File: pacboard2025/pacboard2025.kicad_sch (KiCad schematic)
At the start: 31 parts, among them J1 XT30 Male Connector, U2 D24V50F5, U3 ProS3

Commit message: some more changes
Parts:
- renumbered INTR_TOF to INTR_TOF1, XSHUT_TOF to XSHUT_TOF1
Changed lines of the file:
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@@
 		(on_board yes)
 		(dnp no)
-		(property "Reference" "INTR_TOF"
+		(property "Reference" "INTR_TOF1"
 			(at 35.306 140.716 0)
 			(effects
@@
 			(project "pacboard2025"
 				(path "/8e380e0f-b63e-4626-b5ee-6ded4a9a683b"
-					(reference "INTR_TOF")
+					(reference "INTR_TOF1")
 					(unit 1)
 				)
@@
 		(on_board yes)
 		(dnp no)
-		(property "Reference" "XSHUT_TOF"
+		(property "Reference" "XSHUT_TOF1"
 			(at 30.734 118.872 0)
 			(effects
@@
 			(project "pacboard2025"
 				(path "/8e380e0f-b63e-4626-b5ee-6ded4a9a683b"
-					(reference "XSHUT_TOF")
-					(unit 1)
-				)
+					(reference "XSHUT_TOF1")
+					(unit 1)
+				)

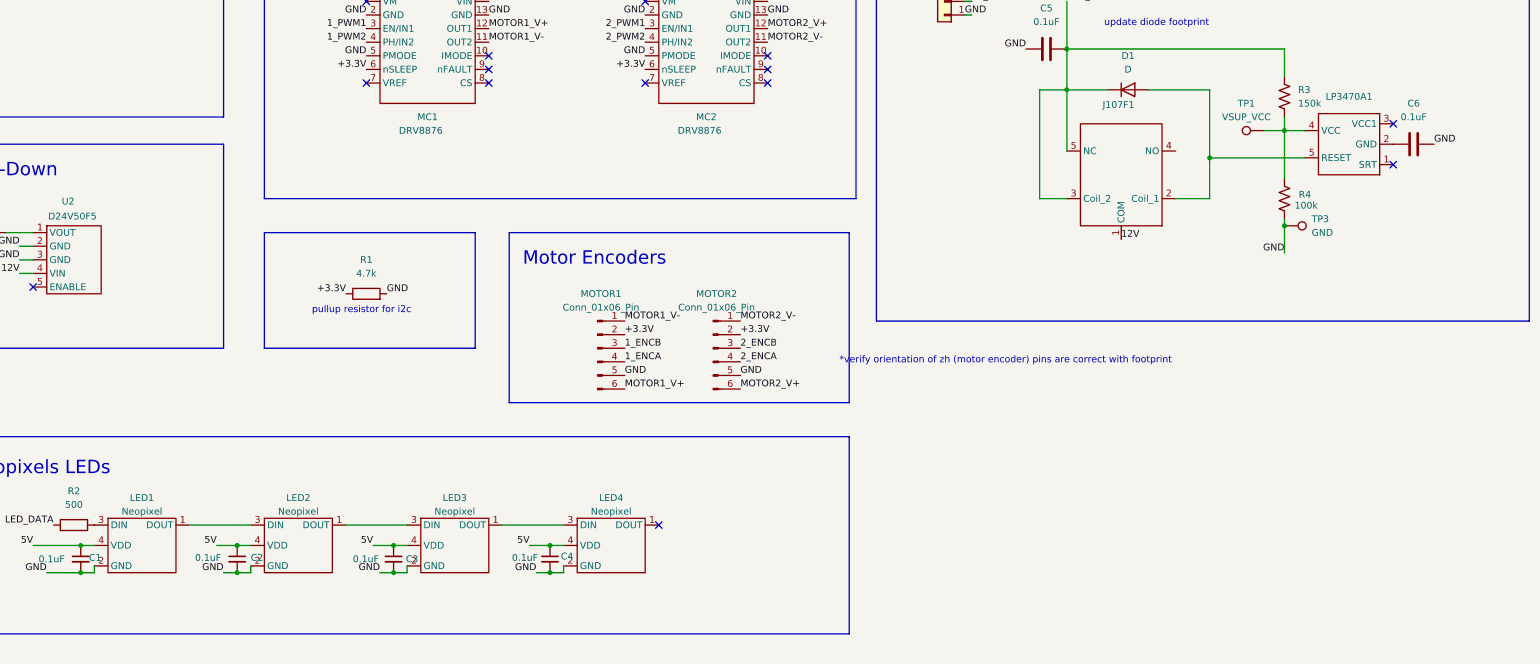
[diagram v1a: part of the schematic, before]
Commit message: fixed neopixels, all ready to go?
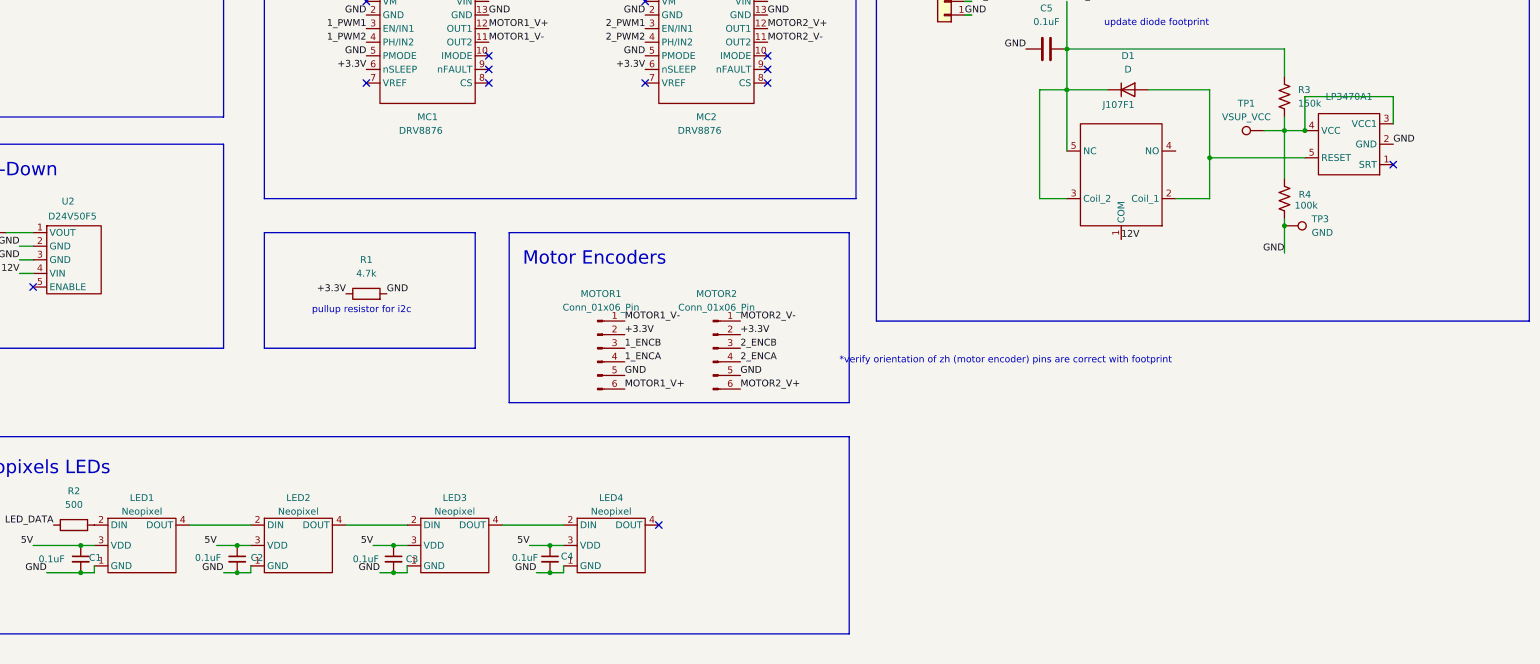
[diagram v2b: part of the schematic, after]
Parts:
- removed C6: 0.1uF, Capacitor_SMD:C_0805_2012Metric_Pad1.18x1.45mm_HandSolder, symbol Device:C
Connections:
- net 5V: now also LED1.3 (VDD), LED2.3 (VDD), LED3.3 (VDD), LED4.3 (VDD); no longer LED1.4 (VDD), LED2.4 (VDD), LED3.4 (VDD), LED4.4 (VDD)
- net GND: now also LED1.1 (GND), LED2.1 (GND), LED3.1 (GND), LED4.1 (GND), LP3470A1.2 (GND); no longer LED1.2 (GND), LED2.2 (GND), LED3.2 (GND), LED4.2 (GND)
- net at R2.2: now also LED1.2 (DIN); no longer LED1.3 (DIN)
- net at LP3470A1.4 (VCC), R3.2, R4.1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: now also LP3470A1.3 (VCC1)
- new net: LED2.4 (DOUT), LED3.2 (DIN)
- new net: LED3.4 (DOUT), LED4.2 (DIN)
- new net: LED1.4 (DOUT), LED2.2 (DIN)
- no-connect marks 19 -> 18
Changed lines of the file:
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@@
 	)
 	(junction
+		(at 359.41 62.23)
+		(diameter 0)
+		(color 0 0 0 0)
+	)
+	(junction
 		(at 130.81 144.78)
 		(diameter 0)
@@
 	)
 	(no_connect
-		(at 375.92 60.96)
-	)
-	(no_connect
 		(at 236.22 53.34)
 	)
@@
 	(wire
 		(pts
+			(xy 375.92 60.96) (xy 375.92 55.88)
+		)
+		(stroke
+			(width 0)
+			(type default)
+		)
+	)
+	(wire
+		(pts
 			(xy 121.92 83.82) (xy 119.38 83.82)
 		)
@@
 	(wire
 		(pts
+			(xy 375.92 55.88) (xy 359.41 55.88)
+		)
+		(stroke
+			(width 0)
+			(type default)
+		)
+	)
+	(wire
+		(pts
 			(xy 105.41 81.28) (xy 109.22 81.28)
 		)
@@
 	(wire
 		(pts
+			(xy 359.41 55.88) (xy 359.41 62.23)
+		)
+		(stroke
+			(width 0)
+			(type default)
+		)
+	)
+	(wire
+		(pts
 			(xy 341.63 67.31) (xy 341.63 74.93)
 		)
@@
 	)
 	(label "GND"
-		(at 383.54 64.77 0)
+		(at 375.92 64.77 0)
 		(fields_autoplaced yes)
 		(effects
@@
 	)
 	(symbol
-		(lib_id "Device:C")
-		(at 379.73 64.77 90)
-		(unit 1)
-		(exclude_from_sim no)
-		(in_bom yes)
-		(on_board yes)
-		(dnp no)
-		(fields_autoplaced yes)
-		(property "Reference" "C6"
-			(at 379.73 57.15 90)
-			(effects
-				(font
-					(size 1.27 1.27)
-				)
-			)
-		)
-		(property "Value" "0.1uF"
-			(at 379.73 59.69 90)
-			(effects
-				(font
-					(size 1.27 1.27)
-				)
-			)
-		)
-		(property "Footprint" "Capacitor_SMD:C_0805_2012Metric_Pad1.18x1.45mm_HandSolder"
-			(at 383.54 63.8048 0)
-			(effects
-				(font
-					(size 1.27 1.27)
-				)
-				(hide yes)
-			)
-		)
-		(property "Datasheet" "~"
-			(at 379.73 64.77 0)
-			(effects
-				(font
-					(size 1.27 1.27)
-				)
-				(hide yes)
-			)
-		)
-		(property "Description" "Unpolarized capacitor"
-			(at 379.73 64.77 0)
-			(effects
-				(font
-					(size 1.27 1.27)
-				)
-				(hide yes)
-			)
-		)
-		(pin "1"
-		)
-		(pin "2"
-		)
-		(instances
-			(project "pacboard2025"
-				(path "/8e380e0f-b63e-4626-b5ee-6ded4a9a683b"
-					(reference "C6")
-					(unit 1)
-				)
-			)
-		)
-	)
-	(symbol
 		(lib_id "Device:R")
 		(at 184.15 92.71 90)
@@
 	)
 	(symbol
+		(lib_name "Neopixel_1")
 		(lib_id "board1_libs:Neopixel")
 		(at 142.24 132.08 0)

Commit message: some more misc changes
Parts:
- LED1, LED2, LED3, LED4: footprint board1_footprints:Neopixel -> board1_footprints:Neopixels 5050
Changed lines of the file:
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@@
 			)
 		)
-		(property "Footprint" "board1_footprints:Neopixel"
+		(property "Footprint" "board1_footprints:Neopixels 5050"
 			(at 200.66 132.08 0)
 			(effects
@@
 			)
 		)
-		(property "Footprint" "board1_footprints:Neopixel"
+		(property "Footprint" "board1_footprints:Neopixels 5050"
 			(at 171.45 132.08 0)
 			(effects
@@
 			)
 		)
-		(property "Footprint" "board1_footprints:Neopixel"
+		(property "Footprint" "board1_footprints:Neopixels 5050"
 			(at 142.24 132.08 0)
 			(effects
@@
 			)
 		)
-		(property "Footprint" "board1_footprints:Neopixel"
+		(property "Footprint" "board1_footprints:Neopixels 5050"
 			(at 229.87 132.08 0)
 			(effects

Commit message: jonathan change bms
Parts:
- D2: footprint board1_footprints:SOD-123FL -> Diode_SMD:D_SMB
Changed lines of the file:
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@@
 			)
 		)
-		(property "Footprint" "board1_footprints:SOD-123FL"
+		(property "Footprint" "Diode_SMD:D_SMB"
 			(at 113.03 81.28 0)
 			(effects

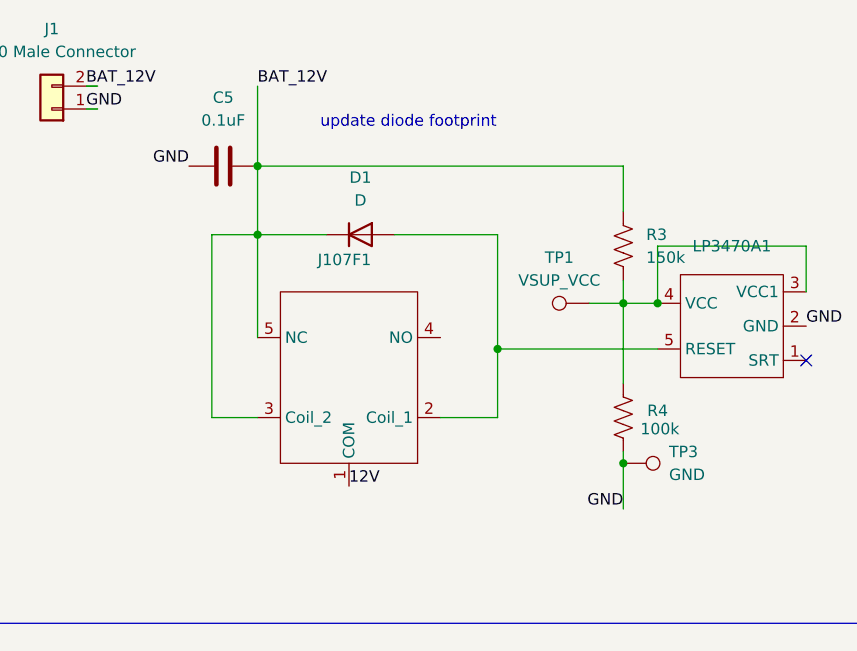
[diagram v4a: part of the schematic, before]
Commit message: updated bms schematic and layout
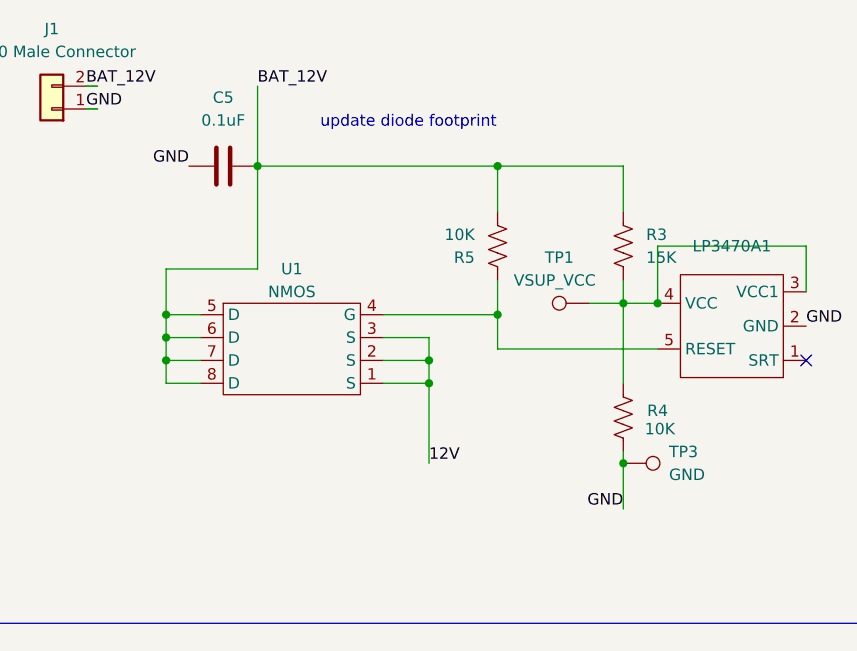
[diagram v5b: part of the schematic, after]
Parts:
- removed D1: D, board1_footprints:SOD-123FL, symbol Device:D
- removed J107F1: ~, board1_footprints:J107, symbol board1_libs:J107F
- added R5: 10K, Resistor_SMD:R_0805_2012Metric_Pad1.20x1.40mm_HandSolder, symbol Device:R_US
- added U1: NMOS, board1_footprints:IFX-PG-TSDSON-8-901-G-V, symbol board1_libs:IRLHM620PbF
- R3: value 150k -> 15K
- R4: value 100k -> 10K
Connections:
- net 12V: now also U1.1 (S), U1.2 (S), U1.3 (S)
- net BAT_12V: now also R5.2, U1.5 (D), U1.6 (D), U1.7 (D), U1.8 (D)
- net at LP3470A1.5 (RESET): now also R5.1, U1.4 (G)

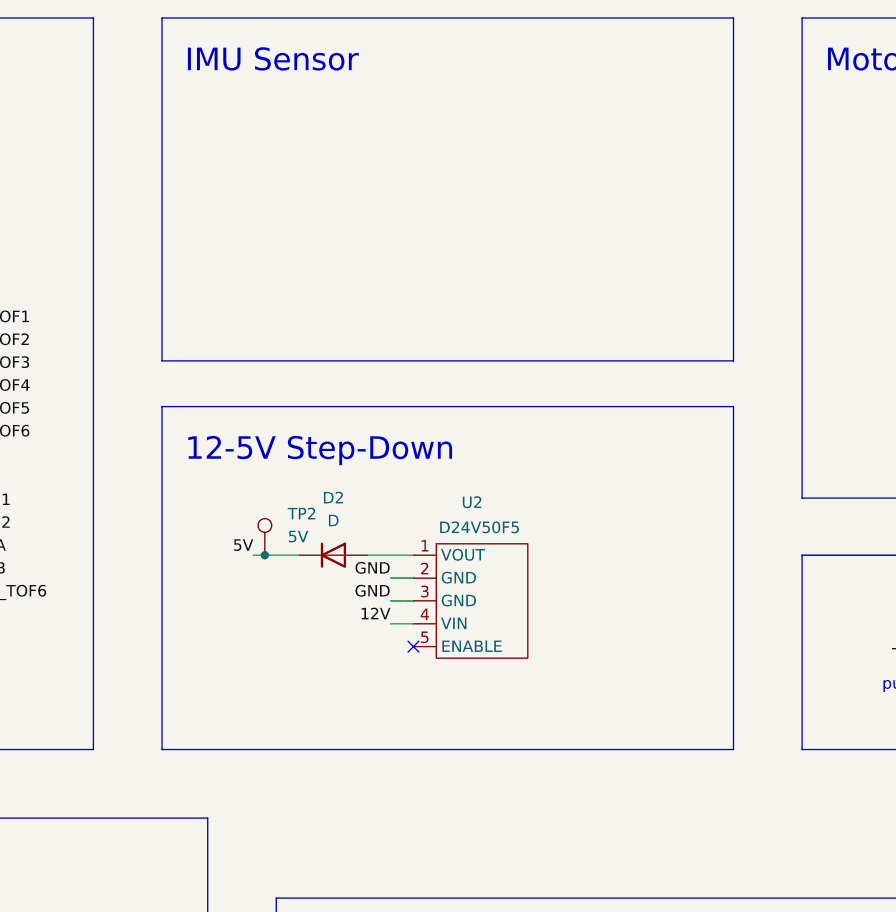
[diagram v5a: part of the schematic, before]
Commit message: final changes, pcb ordered
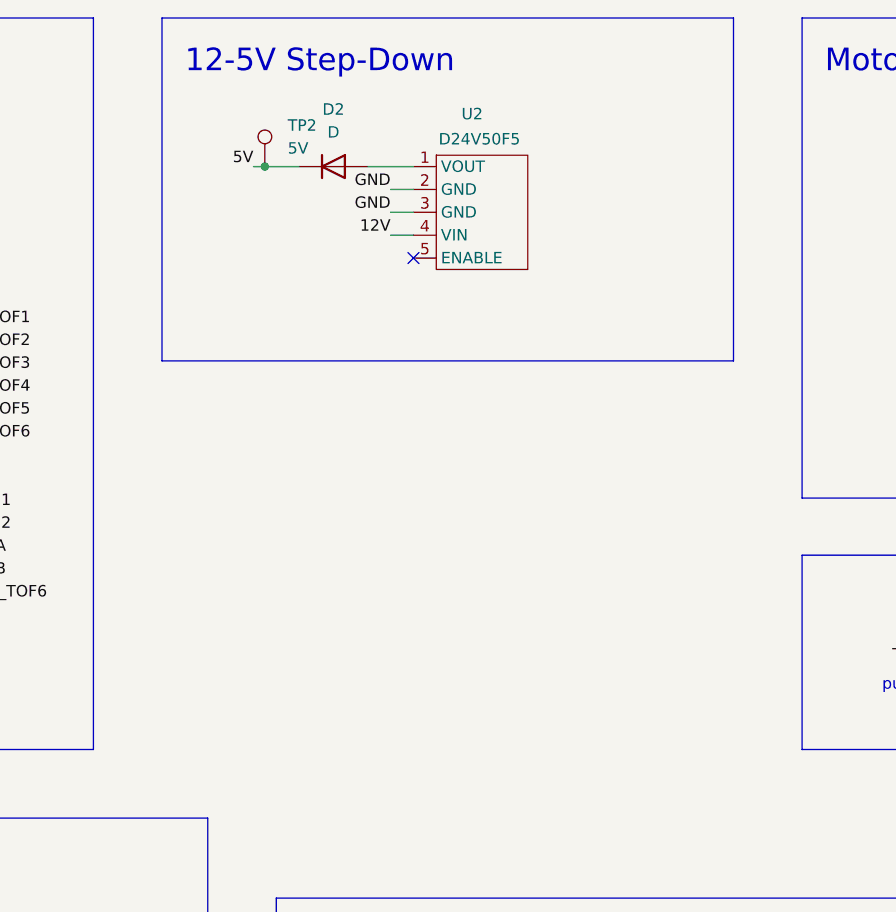
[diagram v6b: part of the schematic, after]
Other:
- note removed: "IMU Sensor"
- moved on the sheet: D2, TP2, U2
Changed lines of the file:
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@@
 	)
 	(junction
-		(at 105.41 81.28)
+		(at 105.41 38.1)
 		(diameter 0)
 		(color 0 0 0 0)
@@
 	)
 	(no_connect
-		(at 121.92 91.44)
+		(at 121.92 48.26)
 	)
 	(no_connect
@@
 	(wire
 		(pts
-			(xy 121.92 86.36) (xy 119.38 86.36)
+			(xy 121.92 43.18) (xy 119.38 43.18)
 		)
 		(stroke
@@
 	(wire
 		(pts
-			(xy 121.92 83.82) (xy 119.38 83.82)
+			(xy 121.92 40.64) (xy 119.38 40.64)
 		)
 		(stroke
@@
 	(wire
 		(pts
-			(xy 121.92 88.9) (xy 119.38 88.9)
+			(xy 121.92 45.72) (xy 119.38 45.72)
 		)
 		(stroke
@@
 	(wire
 		(pts
-			(xy 116.84 81.28) (xy 121.92 81.28)
+			(xy 116.84 38.1) (xy 121.92 38.1)
 		)
 		(stroke
@@
 	(wire
 		(pts
-			(xy 104.14 81.28) (xy 105.41 81.28)
+			(xy 104.14 38.1) (xy 105.41 38.1)
 		)
 		(stroke
@@
 	(wire
 		(pts
-			(xy 105.41 81.28) (xy 109.22 81.28)
+			(xy 105.41 38.1) (xy 109.22 38.1)
 		)
 		(stroke
@@
 	)
 	(rectangle
-		(start 93.98 64.77)
-		(end 157.48 102.87)
+		(start 93.98 21.59)
+		(end 157.48 59.69)
 		(stroke
 			(width 0)
@@
 		)
 	)
-	(rectangle
-		(start 93.98 21.59)
-		(end 157.48 59.69)
-		(stroke
-			(width 0)
-			(type default)
-		)
-		(fill
-			(type none)
-		)
-	)
 	(text "ESP32 ProS3\n"
 		(exclude_from_sim no)
@@
 		)
 	)
-	(text "IMU Sensor"
-		(exclude_from_sim no)
-		(at 96.52 27.94 0)
-		(effects
-			(font
-				(size 2.5 2.5)
-			)
-			(justify left bottom)
-		)
-	)
 	(text "12-5V Step-Down"
 		(exclude_from_sim no)
-		(at 96.52 71.12 0)
+		(at 96.52 27.94 0)
 		(effects
 			(font
@@
 	)
 	(label "GND"
-		(at 119.38 86.36 180)
+		(at 119.38 43.18 180)
 		(fields_autoplaced yes)
 		(effects
@@
 	)
 	(label "12V"
-		(at 119.38 88.9 180)
+		(at 119.38 45.72 180)
 		(fields_autoplaced yes)
 		(effects
@@
 	)
 	(label "GND"
-		(at 119.38 83.82 180)
+		(at 119.38 40.64 180)
 		(fields_autoplaced yes)
 		(effects
@@
 	)
 	(label "5V"
-		(at 104.14 81.28 180)
+		(at 104.14 38.1 180)
 		(fields_autoplaced yes)
 		(effects
@@
 	(symbol
 		(lib_id "Connector:TestPoint")
-		(at 105.41 81.28 0)
+		(at 105.41 38.1 0)
 		(unit 1)
 		(exclude_from_sim no)
@@
 		(fields_autoplaced yes)
 		(property "Reference" "TP2"
-			(at 107.95 76.7079 0)
+			(at 107.95 33.5279 0)
 			(effects
 				(font
@@
 		)
 		(property "Value" "5V"
-			(at 107.95 79.2479 0)
+			(at 107.95 36.0679 0)
 			(effects
 				(font
@@
 		)
 		(property "Footprint" "Connector_PinHeader_2.54mm:PinHeader_1x01_P2.54mm_Vertical"
-			(at 110.49 81.28 0)
+			(at 110.49 38.1 0)
 			(effects
 				(font
@@
 		)
 		(property "Datasheet" "~"
-			(at 110.49 81.28 0)
+			(at 110.49 38.1 0)
 			(effects
 				(font
@@
 		)
 		(property "Description" "test point"
-			(at 105.41 81.28 0)
+			(at 105.41 38.1 0)
 			(effects
 				(font
@@
 	(symbol
 		(lib_id "board1_libs:D24V50F5")
-		(at 129.54 81.28 0)
+		(at 129.54 38.1 0)
 		(unit 1)
 		(exclude_from_sim no)
@@
 		(dnp no)
 		(property "Reference" "U2"
-			(at 127.254 75.438 0)
+			(at 127.254 32.258 0)
 			(effects
 				(font
@@
 		)
 		(property "Value" "D24V50F5"
-			(at 124.714 78.232 0)
+			(at 124.714 35.052 0)
 			(effects
 				(font
@@
 		)
 		(property "Footprint" "Connector_PinHeader_2.54mm:PinHeader_1x05_P2.54mm_Vertical"
-			(at 128.27 81.28 0)
+			(at 128.27 38.1 0)
 			(effects
 				(font
@@
 		)
 		(property "Datasheet" ""
-			(at 128.27 81.28 0)
+			(at 128.27 38.1 0)
 			(effects
 				(font
@@
 		)
 		(property "Description" ""
-			(at 129.54 81.28 0)
+			(at 129.54 38.1 0)
 			(effects
 				(font
@@
 	(symbol
 		(lib_id "Device:D")
-		(at 113.03 81.28 0)
+		(at 113.03 38.1 0)
 		(unit 1)
 		(exclude_from_sim no)
@@
 		(fields_autoplaced yes)
 		(property "Reference" "D2"
-			(at 113.03 74.93 0)
+			(at 113.03 31.75 0)
 			(effects
 				(font
@@
 		)
 		(property "Value" "D"
-			(at 113.03 77.47 0)
+			(at 113.03 34.29 0)
 			(effects
 				(font
@@
 		)
 		(property "Footprint" "Diode_SMD:D_SMB"
-			(at 113.03 81.28 0)
+			(at 113.03 38.1 0)
 			(effects
 				(font
@@
 		)
 		(property "Datasheet" "~"
-			(at 113.03 81.28 0)
+			(at 113.03 38.1 0)
 			(effects
 				(font
@@
 		)
 		(property "Description" "Diode"
-			(at 113.03 81.28 0)
+			(at 113.03 38.1 0)
 			(effects
 				(font
@@
 		)
 		(property "Sim.Device" "D"
-			(at 113.03 81.28 0)
+			(at 113.03 38.1 0)
 			(effects
 				(font
@@
 		)
 		(property "Sim.Pins" "1=K 2=A"
-			(at 113.03 81.28 0)
+			(at 113.03 38.1 0)
 			(effects
 				(font
